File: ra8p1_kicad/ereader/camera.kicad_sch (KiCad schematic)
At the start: 7 parts, among them J3 1-1734248-5, U24 SN74LVC1G97DBVR

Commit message: docs(hardware): expand camera sheet and reconcile interface reservations
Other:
- note added: "CMS-014 / CMS-015: Pcam 5C, 2-lane CSI-2 to VIN0 U24: PWUP = CAM_PWR_REQ AND MCU_RESET_N. PWUP low >=100ms; then high >=50ms before SCCB. Qualification and second-camera/lighting work remain open. See ../design/camera_storage_interfaces.md, CMS-014..016."
- moved on the sheet: C112, J3, R96, R97, R98, R99, U24

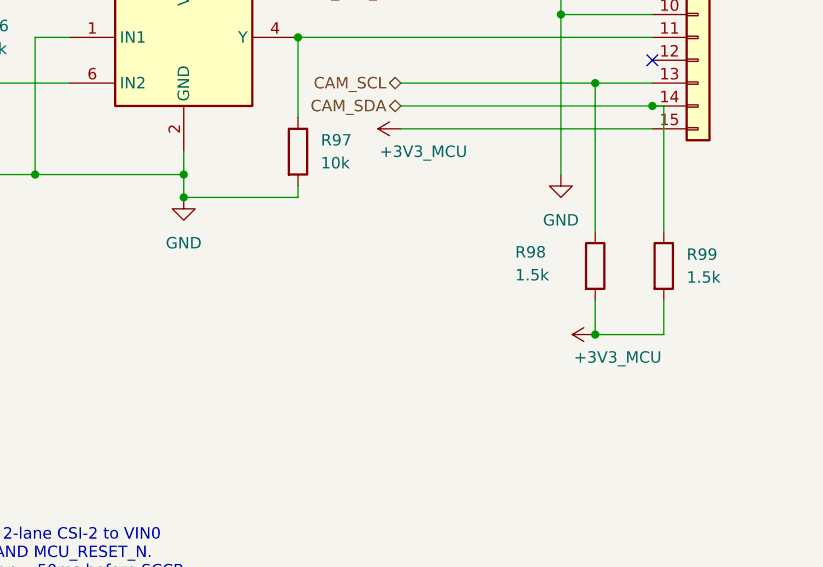
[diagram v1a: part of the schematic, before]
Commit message: wip(hardware): preserve schematic cleanup and CEU host ports
Checkpoint cosmetic cleanup across the schematic hierarchy and eleven parallel-camera host ports. Refresh the complete 13-page PDF. All 334 existing net partitions and 271 component records match the prior CEU checkpoint; all 128 ERC identities remain unchanged. Electrical design is incomplete; this is a WIP checkpoint for #821 and #841.
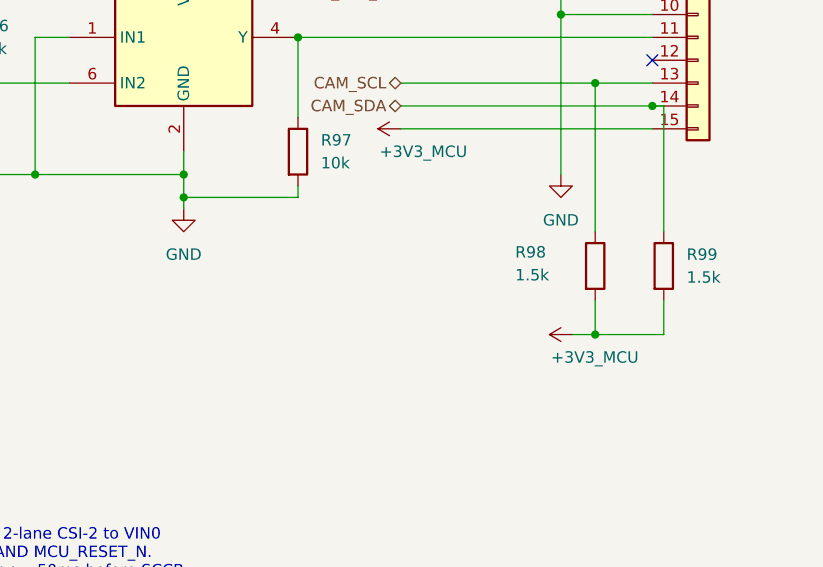
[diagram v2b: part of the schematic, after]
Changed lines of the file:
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@@
+	(wire
+		(pts
+			(xy 113.03 90.17) (xy 113.03 88.9)
+		)
+		(stroke
+			(width 0)
+			(type default)
+		)
+	)
 	(wire
 		(pts
@@
 		(pts
 			(xy 87.63 86.36) (xy 96.52 86.36)
+		)
+		(stroke
+			(width 0)
+			(type default)
+		)
+	)
+	(wire
+		(pts
+			(xy 156.21 104.14) (xy 158.75 104.14)
 		)
 		(stroke
@@
 	(symbol
 		(lib_id "power:GND")
-		(at 113.03 88.9 0)
+		(at 113.03 90.17 0)
 		(unit 1)
 		(body_style 1)
@@
 		(fields_autoplaced yes)
 		(property "Reference" "#PWR0223"
+			(at 113.03 96.52 0)
+			(hide yes)
+			(show_name no)
+			(do_not_autoplace no)
+			(effects
+				(font
+					(size 1.27 1.27)
+				)
+			)
+		)
+		(property "Value" "GND"
 			(at 113.03 95.25 0)
-			(hide yes)
-			(show_name no)
-			(do_not_autoplace no)
-			(effects
-				(font
-					(size 1.27 1.27)
-				)
-			)
-		)
-		(property "Value" "GND"
-			(at 113.03 93.98 0)
 			(show_name no)
 			(do_not_autoplace no)
@@
 		)
 		(property "Footprint" ""
-			(at 113.03 88.9 0)
+			(at 113.03 90.17 0)
 			(hide yes)
 			(show_name no)
@@
 		)
 		(property "Datasheet" ""
-			(at 113.03 88.9 0)
+			(at 113.03 90.17 0)
 			(hide yes)
 			(show_name no)
@@
 		)
 		(property "Description" "Power symbol creates a global label with name \"GND\" , ground"
-			(at 113.03 88.9 0)
+			(at 113.03 90.17 0)
 			(hide yes)
 			(show_name no)
@@
 	(symbol
 		(lib_id "power:+3V3")
-		(at 158.75 104.14 90)
+		(at 156.21 104.14 90)
 		(unit 1)
 		(body_style 1)
@@
 		(dnp no)
 		(property "Reference" "#PWR0227"
-			(at 162.56 104.14 0)
+			(at 160.02 104.14 0)
 			(hide yes)
 			(show_name no)
@@
 		)
 		(property "Value" "+3V3_MCU"
-			(at 166.116 106.68 90)
+			(at 163.576 106.68 90)
 			(show_name no)
 			(do_not_autoplace yes)
@@
 		)
 		(property "Footprint" ""
-			(at 158.75 104.14 0)
+			(at 156.21 104.14 0)
 			(hide yes)
 			(show_name no)
@@
 		)
 		(property "Datasheet" ""
-			(at 158.75 104.14 0)
+			(at 156.21 104.14 0)
 			(hide yes)
 			(show_name no)
@@
 		)
 		(property "Description" "Power symbol creates a global label with name \"+3V3\""
-			(at 158.75 104.14 0)
-			(hide yes)
-			(show_name no)
+			(at 156.21 104.14 0)
+			(hide yes)
+			(show_name no)
